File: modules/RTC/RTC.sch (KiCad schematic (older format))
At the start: 26 parts, among them J1 2, J10 11, J11 12, J12 13, J13 A0, J14 A1, J15 A2, J16 A3, J17 A4, J18 A5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

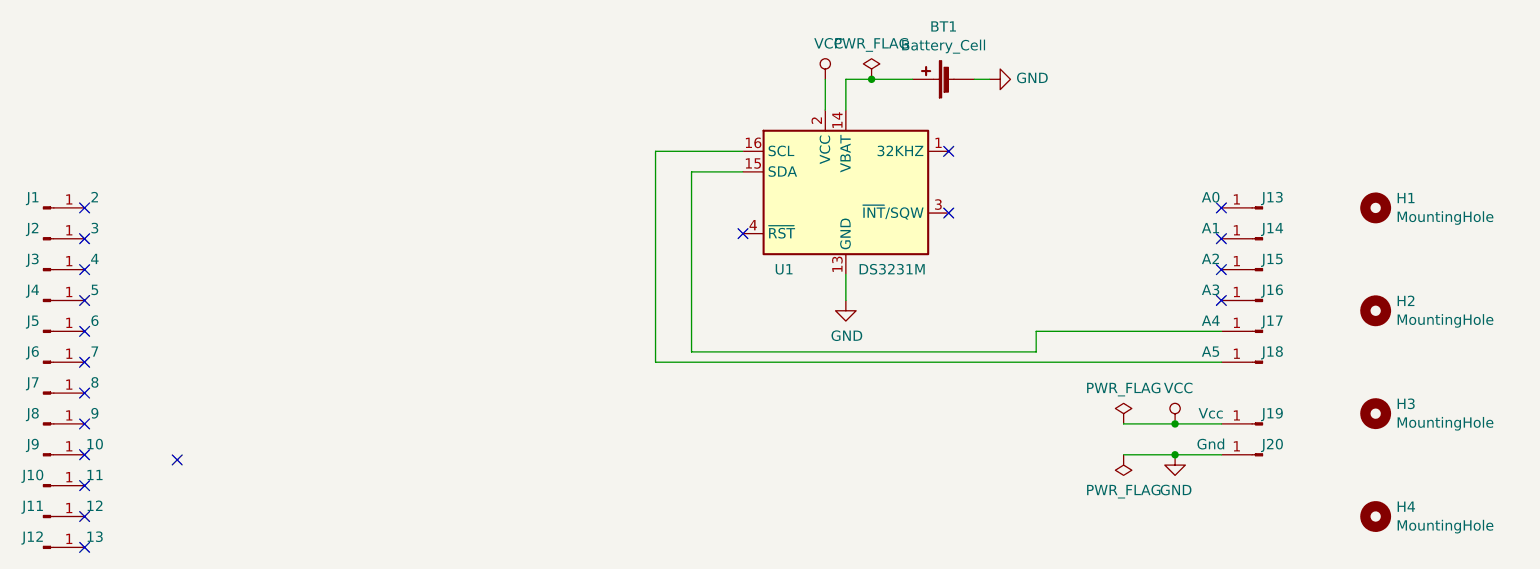
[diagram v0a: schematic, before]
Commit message: RTC pcb + CR1220 holder
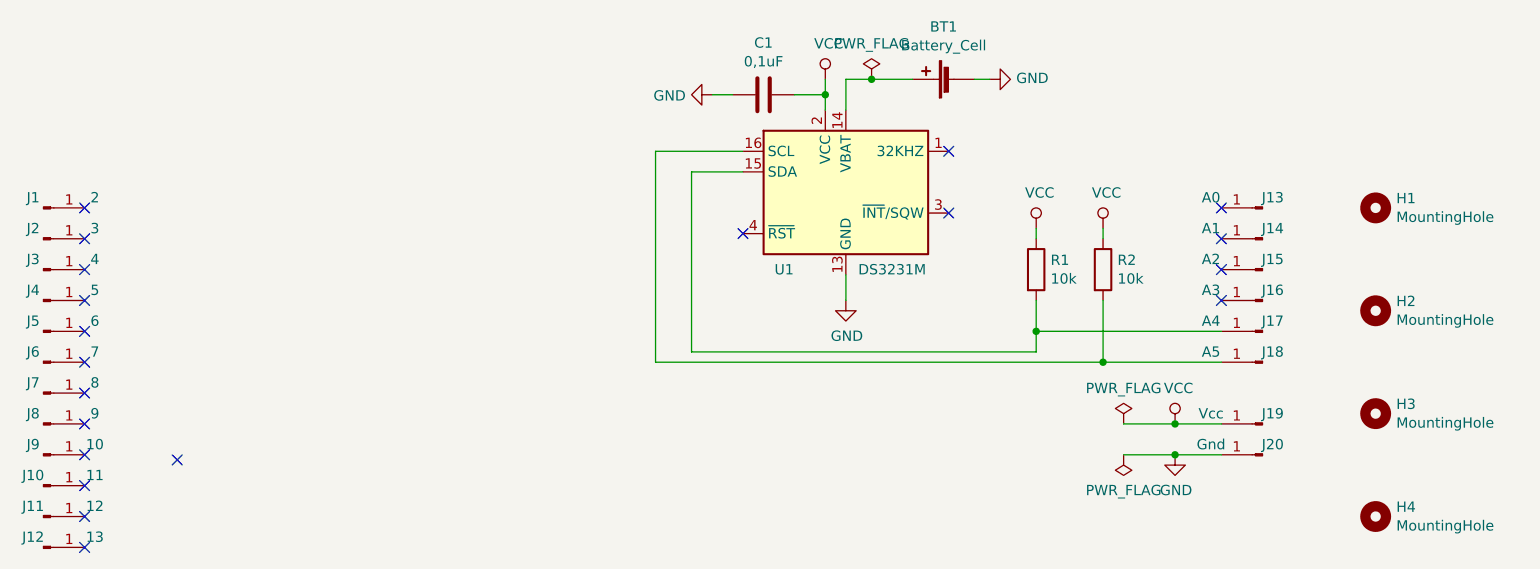
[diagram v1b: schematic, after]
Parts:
- added C1: 0,1uF, Capacitor_SMD:C_0805_2012Metric_Pad1.15x1.40mm_HandSolder, symbol Device:C
- added R1, R2: 10k, Resistor_SMD:R_0805_2012Metric_Pad1.15x1.40mm_HandSolder, symbol Device:R
- BT1: footprint Battery:BatteryHolder_Keystone_500 -> CommonLibrary:CR1220-holder
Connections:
- net GND: now also C1.2
- net VCC: now also C1.1, R1.1, R2.1
- net at J17.1 (Pin_1), U1.15 (SDA): now also R1.2
- net at J18.1 (Pin_1), U1.16 (SCL): now also R2.2
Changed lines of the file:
@@
 F 0 "BT1" V 5705 1925 50  0000 C CNN
 F 1 "Battery_Cell" V 5614 1925 50  0000 C CNN
-F 2 "Battery:BatteryHolder_Keystone_500" V 5450 1935 50  0001 C CNN
+F 2 "CommonLibrary:CR1220-holder" V 5450 1935 50  0001 C CNN
 F 3 "~" V 5450 1935 50  0001 C CNN
 	1    5450 1875
@@
 	4925 1875 5050 1875
 Wire Wire Line
-	4825 1875 4825 2025
+	4825 1875 4825 1950
 Wire Wire Line
 	4425 2225 4000 2225
@@
 	4000 2225 4000 3250
 Wire Wire Line
-	4000 3250 6750 3250
+	4000 3250 6175 3250
 Wire Wire Line
 	4425 2325 4175 2325
@@
 Wire Wire Line
 	5050 1875 5250 1875
+$Comp
+L Device:R R1
+U 1 1 5D89F47E
+P 5850 2800
+F 0 "R1" H 5920 2846 50  0000 L CNN
+F 1 "10k" H 5920 2755 50  0000 L CNN
+F 2 "Resistor_SMD:R_0805_2012Metric_Pad1.15x1.40mm_HandSolder" V 5780 2800 50  0001 C CNN
+F 3 "~" H 5850 2800 50  0001 C CNN
+	1    5850 2800
+	1    0    0    -1
+$EndComp
+$Comp
+L Device:R R2
+U 1 1 5D89FC60
+P 6175 2800
+F 0 "R2" H 6245 2846 50  0000 L CNN
+F 1 "10k" H 6245 2755 50  0000 L CNN
+F 2 "Resistor_SMD:R_0805_2012Metric_Pad1.15x1.40mm_HandSolder" V 6105 2800 50  0001 C CNN
+F 3 "~" H 6175 2800 50  0001 C CNN
+	1    6175 2800
+	1    0    0    -1
+$EndComp
+Wire Wire Line
+	5850 2950 5850 3100
+Connection ~ 5850 3100
+Wire Wire Line
+	6175 2950 6175 3250
+Connection ~ 6175 3250
+Wire Wire Line
+	6175 3250 6750 3250
+$Comp
+L power:VCC #PWR01001
+U 1 1 5D8A0B49
+P 5850 2600
+F 0 "#PWR01001" H 5850 2450 50  0001 C CNN
+F 1 "VCC" H 5867 2773 50  0000 C CNN
+F 2 "" H 5850 2600 50  0001 C CNN
+F 3 "" H 5850 2600 50  0001 C CNN
+	1    5850 2600
+	1    0    0    -1
+$EndComp
+$Comp
+L power:VCC #PWR01002
+U 1 1 5D8A12C8
+P 6175 2600
+F 0 "#PWR01002" H 6175 2450 50  0001 C CNN
+F 1 "VCC" H 6192 2773 50  0000 C CNN
+F 2 "" H 6175 2600 50  0001 C CNN
+F 3 "" H 6175 2600 50  0001 C CNN
+	1    6175 2600
+	1    0    0    -1
+$EndComp
+Wire Wire Line
+	5850 2600 5850 2650
+Wire Wire Line
+	6175 2600 6175 2650
+$Comp
+L Device:C C1
+U 1 1 5D8A5053
+P 4525 1950
+F 0 "C1" V 4273 1950 50  0000 C CNN
+F 1 "0,1uF" V 4364 1950 50  0000 C CNN
+F 2 "Capacitor_SMD:C_0805_2012Metric_Pad1.15x1.40mm_HandSolder" H 4563 1800 50  0001 C CNN
+F 3 "~" H 4525 1950 50  0001 C CNN
+	1    4525 1950
+	0    1    1    0
+$EndComp
+$Comp
+L power:GND #PWR01003
+U 1 1 5D8A5E45
+P 4275 1950
+F 0 "#PWR01003" H 4275 1700 50  0001 C CNN
+F 1 "GND" V 4280 1822 50  0000 R CNN
+F 2 "" H 4275 1950 50  0001 C CNN
+F 3 "" H 4275 1950 50  0001 C CNN
+	1    4275 1950
+	0    1    1    0
+$EndComp
+Wire Wire Line
+	4275 1950 4375 1950
+Wire Wire Line
+	4675 1950 4825 1950
+Connection ~ 4825 1950
+Wire Wire Line
+	4825 1950 4825 2025
 $EndSCHEMATC

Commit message: Add silk
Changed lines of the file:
@@
 P 5050 1875
 F 0 "#FLG0101" H 5050 1950 50  0001 C CNN
-F 1 "PWR_FLAG" H 5050 2048 50  0000 C CNN
+F 1 "PWR_FLAG" H 5125 1800 50  0000 C CNN
 F 2 "" H 5050 1875 50  0001 C CNN
 F 3 "~" H 5050 1875 50  0001 C CNN
